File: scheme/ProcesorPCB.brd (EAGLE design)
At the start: 87.3 x 59.7 mm, 25 parts, among them X1 22-23-2101, X10 22-23-2021, X11 22-23-2021, X12 22-23-2051, X2 22-23-2101, X3 22-23-2101, X4 22-23-2101, X5 22-23-2051, X7 22-23-2021, X8 22-23-2031, X9 22-23-2021

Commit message: Work on PCB
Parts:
- removed X1, X2, X3, X4: 22-23-2101, con-molex:22-23-2101
- removed X10, X11, X7, X9: 22-23-2021, con-molex:22-23-2021
- removed X5: 22-23-2051, con-molex:22-23-2051
- removed X6: (no value), con-ptr500:AK500/2
- removed X8: 22-23-2031, con-molex:22-23-2031
- added JP10, JP11, JP12, JP13, JP14, JP15, JP16, JP17, JP18, JP7, JP8, JP9: (no value), jumper:JP2
- JP1: device jumper:JP4 -> jumper:JP10Q
- moved JP3 23.0 mm to (58.4, 41.9)
- moved JP1 21.0 mm to (78.7, 15.2), turned to 90 degrees
- moved X12 9.92 mm to (14.0, 8.89)
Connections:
- removed net DI: JP1.3, X5.1
- removed net DO: X5.4
- removed net E2: U$1.5, X1.9
- removed net E3: X2.4
- removed net E4: X2.9
- removed net E5: X3.4
- removed net E6: X3.9
- removed net E8: JP1.1, X4.9
- removed net EV11: X2.6
- removed net EV12: X2.8
- removed net EV17: X3.6
- removed net EV18: X3.8
- removed net N$29: X3.10
- removed net Y3: X2.5
- removed net Y4: X2.7
- removed net Y5: X3.5
- removed net Y6: X3.7
- new net CCP: JP1.6, U$1.5
- new net N$7: R1.1
- new net N$9: JP3.3, JP3.4, JP6.1
- net +5V: now also JP1.4; no longer R1.1, R2.1, X10.1, X11.1, X4.1, X6.1, X7.1, X9.1
- net CKL: no longer X5.2
- net E1: no longer X1.4
- net E7: no longer X4.6
- net EV5: no longer X1.6
- net EV6: no longer X1.8
- net GND: now also JP1.10; no longer JP3.3, JP3.4, JP6.1, X10.2, X11.2, X4.2, X5.5, X6.2, X7.2, X8.1, X9.2
- net LD: no longer X5.3
- net PGC,S1: no longer X1.2, X2.2, X3.2, X4.4
- net PGD,S2: no longer X1.1, X2.1, X3.1, X4.3
- net RX: no longer X8.2
- net S0: no longer X1.3, X2.3, X3.3, X4.5
- net SDA: no longer JP1.4
- net SDO: no longer JP1.2
- net TX: no longer X8.3
- net VPP,Y7: no longer X4.7
- net Y1: no longer X1.5
- net Y2: no longer X1.7
- net Y8: no longer X4.8
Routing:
- net GND: track 342.8 -> 0.00 mm, vias 2 -> 0
- net +5V: track 170.4 -> 0.00 mm
- net Y8: track 153.7 -> 0.00 mm
- net E7: track 151.1 -> 0.00 mm
- net VPP,Y7: track 149.9 -> 0.00 mm, vias 2 -> 0
- net E8: track 110.5 -> 0.00 mm, vias 2 -> 0
- net TX: track 95.2 -> 0.00 mm, vias 2 -> 0
- net E2: track 87.6 -> 0.00 mm
- net EV6: track 82.5 -> 0.00 mm
- net N$9: track 0.00 -> 78.7 mm
- net Y2: track 77.5 -> 0.00 mm
- net PGC,S1: track 71.1 -> 0.00 mm
- net PGD,S2: track 63.5 -> 0.00 mm
- net RX: track 76.2 -> 24.1 mm, vias 2 -> 0
- net S0: track 49.5 -> 0.00 mm
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
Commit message: Hmm not Saved
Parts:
- added U1: UA78L05ACPKG3, TI-Eagle_library:SOT150P400X160-4N
- added X1: 22-23-2031, con-molex:22-23-2031
- moved LED3 55.7 mm to (25.4, 26.7)
- moved R3 53.4 mm to (31.8, 28.6)
- moved JP3 23.0 mm to (35.6, 44.5), turned to 90 degrees
- moved JP1 1.27 mm to (77.5, 15.2)
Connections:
- removed net CKL: U$1.11
- removed net E1: U$1.16
- removed net E7: U$1.3
- removed net EV5: U$1.14
- removed net LD: U$1.8
- removed net N$7: R1.1
- removed net PGC,S1: U$1.18, X12.4
- removed net PGD,S2: U$1.19, X12.3
- removed net S0: U$1.17
- removed net SDA: U$1.13
- removed net SDO: U$1.9
- removed net Y1: U$1.15
- removed net Y2: U$1.7
- new net +24V: U1.3, X1.3
- new net AN0,PGD: JP7.2, U$1.19, X12.3
- new net AN1,PGC: JP8.2, U$1.18, X12.4
- new net AN10: JP17.2, U$1.13
- new net AN11: JP18.2, U$1.12
- new net AN2: JP9.2, U$1.17
- new net AN3: JP10.2, U$1.3
- new net AN4: JP11.2, U$1.16
- new net AN5: JP12.2, U$1.15
- new net AN6: JP13.2, U$1.14
- new net AN7: JP14.2, U$1.7
- new net AN8: JP15.2, U$1.8
- new net AN9: JP16.2, U$1.9
- new net OUT: U$1.11, X1.2
- net +5V: now also JP10.1, JP11.1, JP12.1, JP13.1, JP14.1, JP15.1, JP16.1, JP17.1, JP18.1, JP7.1, JP8.1, JP9.1, U1.1; no longer JP4.1, LED3.A
- net GND: now also JP10.3, JP11.3, JP12.3, JP13.3, JP14.3, JP15.3, JP16.3, JP17.3, JP18.3, JP7.3, JP8.3, JP9.3, U1.2, U1.4, X1.1; no longer R3.1
- net RX: no longer U$1.12
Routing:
- net GND: track 0.00 -> 63.5 mm
- net +5V: track 0.00 -> 51.3 mm
- net N$9: track 78.7 -> 58.6 mm
- net N$2: track 54.7 -> 35.6 mm
- net +24V: track 0.00 -> 16.8 mm
- net CCP: track 0.00 -> 12.7 mm
- net OUT: track 0.00 -> 10.2 mm
- net N$8: track 3.39 -> 0.00 mm

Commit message: PCB borad almost finished.
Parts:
- removed JP3, JP5, JP6: (no value), jumper:JP4
- removed JP4: (no value), jumper:JP1
- removed LED1: Cervena, led:LED5MM
- removed LED2, LED3: Zenena, led:LED5MM
- removed R2, R3: (no value), rcl:R0805W
- added C1: 1uF, resistor:C025-030X050
- added C2: 0.33uF, resistor:C025-030X050
- added RN1, RN2: 15K, resistor-net:RN-7
- added RN3: 22k, resistor-net:RN-7
- added RN4: 22K, resistor-net:RN-7
- R1: device rcl:R0805W -> resistor:0207/10
- moved R1 50.6 mm to (52.1, 21.6), flipped to the top, turned to 90 degrees
- moved X12 31.8 mm to (45.7, 10.2)
- moved JP2 22.5 mm to (50.8, 38.1), turned to 270 degrees
- moved X1 10.5 mm to (45.7, 29.2)
- moved JP1 5.08 mm to (82.5, 15.2)
- moved U1 1.80 mm to (57.1, 5.08)
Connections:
- removed net AN11: JP18.2, U$1.12
- removed net N$3: JP6.4, LED2.K
- removed net N$4: JP6.3, LED1.K
- removed net N$5: LED2.A, R2.2
- removed net N$6: LED1.A, R1.2
- removed net N$8: LED3.K, R3.2
- removed net N$9: JP3.3, JP3.4, JP6.1
- removed net RX: JP2.4, JP5.4
- new net AN11,RX: JP18.2, JP2.4, RN1.7, RN3.7, U$1.12
- net +24V: now also R1.2; no longer U1.3
- net +5V: now also C1.1, RN3.1, RN4.1
- net AN0,PGD: now also RN2.7, RN4.7
- net AN1,PGC: now also RN2.6, RN4.6
- net AN10: now also RN1.3, RN3.3
- net AN2: now also RN2.5, RN4.5
- net AN3: now also RN1.2, RN3.2
- net AN4: now also RN2.4, RN4.4
- net AN5: now also RN2.3, RN4.3
- net AN6: now also RN2.2, RN4.2
- net AN7: now also RN1.4, RN3.4
- net AN8: now also RN1.5, RN3.5
- net AN9: now also RN1.6, RN3.6
- net GND: now also C1.2, C2.2, JP2.2, RN1.1, RN2.1
- net N$2: now also C2.1, R1.1, U1.3; no longer JP3.1, JP3.2, JP4.2, JP6.2
- net TX: no longer JP5.3
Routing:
- net GND: track 63.5 -> 128.2 mm, vias 0 -> 1
- net N$9: track 58.6 -> 0.00 mm
- net AN10: track 0.00 -> 41.8 mm
- net AN3: track 0.00 -> 40.7 mm
- net AN0,PGD: track 0.00 -> 36.1 mm
- net AN1,PGC: track 0.00 -> 34.3 mm
- net AN2: track 0.00 -> 30.5 mm
- net AN4: track 0.00 -> 30.3 mm
- net AN5: track 0.00 -> 28.8 mm
- net +5V: track 51.3 -> 79.4 mm
- net AN11,RX: track 0.00 -> 25.5 mm
- net AN6: track 0.00 -> 25.5 mm
- net N$3: track 25.4 -> 0.00 mm
- net RX: track 24.1 -> 0.00 mm
- net AN7: track 0.00 -> 23.4 mm
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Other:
- board size 87.3 x 59.7 mm -> 44.1 x 45.7 mm

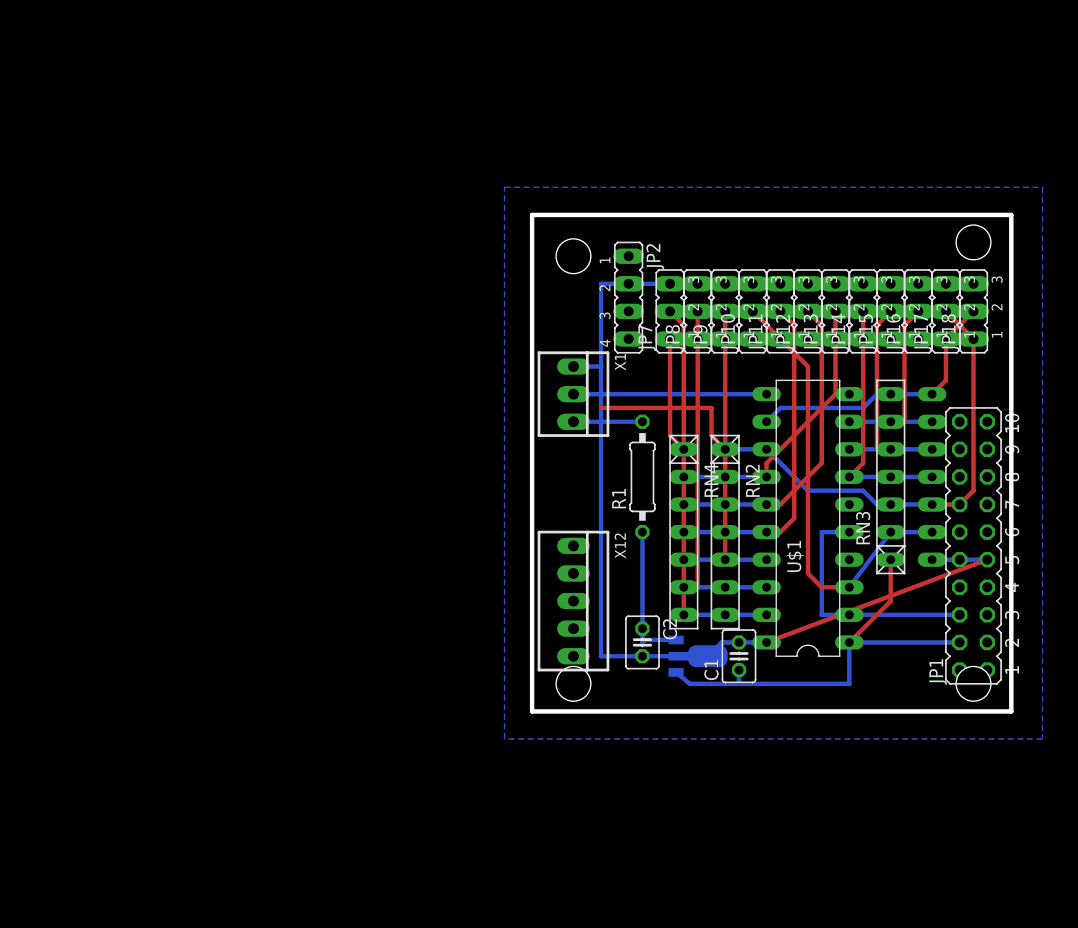
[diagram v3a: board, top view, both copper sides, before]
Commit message: Add documentation for LM358, update schema, add adc settings from previous project to file orig_mail.c
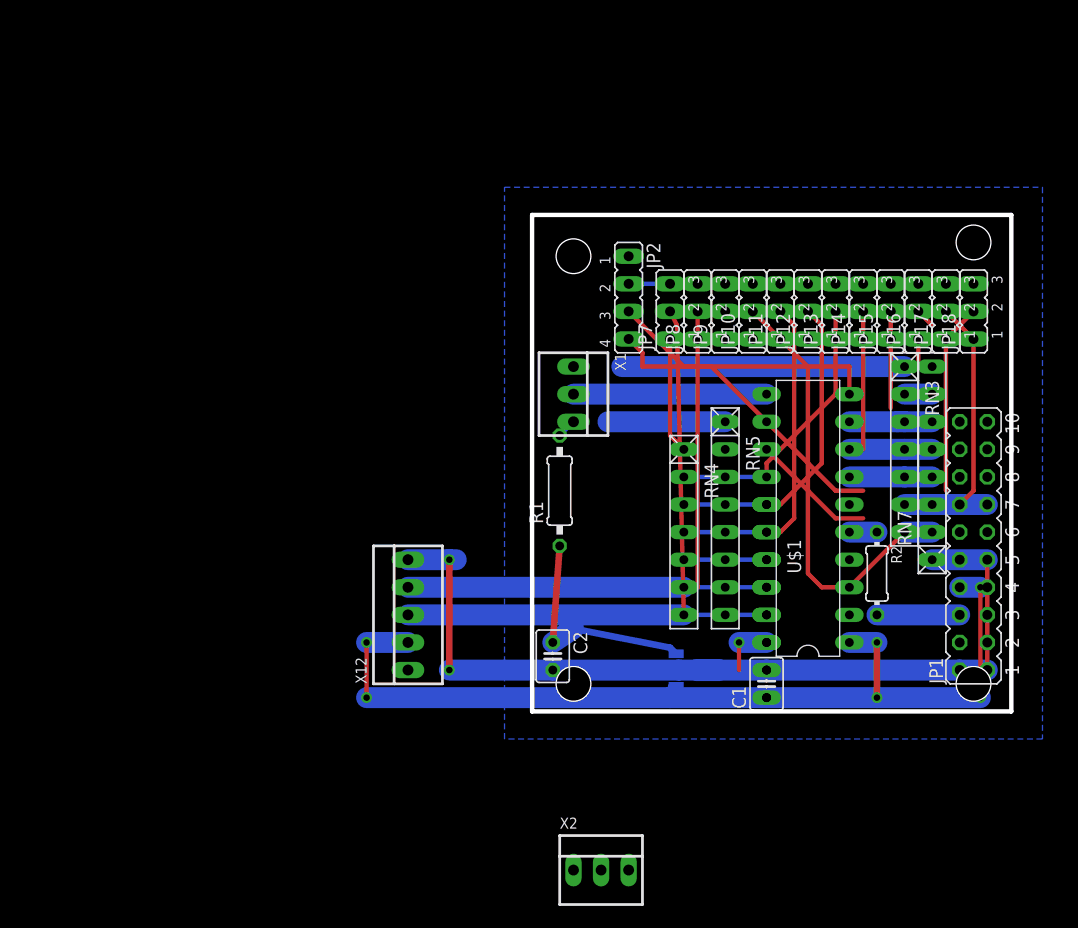
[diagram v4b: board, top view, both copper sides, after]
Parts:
- removed RN2: 15K, resistor-net:RN-7
- added R2: 1k, resistor:0204/7
- added RN5: 15k, resistor-net:RN-8
- added RN7: (no value), resistor-net:RN-8
- added X2: 22-23-2031, con-molex:22-23-2031
- RN1: value 15K -> 15k; device resistor-net:RN-7 -> resistor-net:RN-8
- moved RN1 19.0 mm to (63.5, 10.2), turned to 270 degrees
- moved X12 15.3 mm to (30.5, 8.89), turned to 90 degrees
- moved C2 8.35 mm to (43.8, 5.08)
- moved R1 7.73 mm to (44.5, 20.3)
- moved C1 3.59 mm to (63.5, 2.54)
- moved RN3 2.84 mm to (76.2, 24.1), turned to 270 degrees
- moved U1 1.27 mm to (57.1, 3.81)
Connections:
- new net N$4: JP1.6, R2.2
- net +5V: now also JP1.8, RN1.8; no longer JP1.4
- net AN0,PGD: no longer RN2.7
- net AN1,PGC: no longer RN2.6
- net AN10: now also RN3.6, RN7.3; no longer RN1.3, RN3.3
- net AN11,RX: now also RN3.2, RN7.7, X2.2; no longer RN1.7, RN3.7
- net AN2: no longer RN2.5
- net AN3: now also RN3.7, RN7.2; no longer RN1.2, RN3.2
- net AN4: no longer RN2.4
- net AN5: no longer RN2.3
- net AN6: no longer RN2.2
- net AN7: now also RN3.5, RN7.4; no longer RN1.4, RN3.4
- net AN8: now also RN3.4, RN7.5; no longer RN1.5, RN3.5
- net AN9: now also RN3.3, RN7.6; no longer RN1.6, RN3.6
- net CCP: now also R2.1; no longer JP1.6
- net GND: now also JP1.2, RN1.7, RN5.1, RN7.1, X2.1; no longer JP1.10, RN1.1, RN2.1
- net TX: now also X2.3
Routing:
- net +5V: track 79.4 -> 153.9 mm, vias 0 -> 6
- net AN1,PGC: track 34.3 -> 59.7 mm
- net AN0,PGD: track 36.1 -> 61.1 mm
- net TX: track 0.00 -> 25.0 mm
- net AN2: track 30.5 -> 7.62 mm
- net AN11,RX: track 25.5 -> 48.2 mm
- net CCP: track 22.9 -> 2.54 mm
- net AN9: track 19.6 -> 9.42 mm
- net N$2: track 13.4 -> 21.1 mm
- net N$4: track 0.00 -> 7.62 mm
- net AN8: track 22.1 -> 16.5 mm
- net +24V: track 6.35 -> 1.80 mm
- net AN10: track 41.8 -> 38.5 mm
- net AN7: track 23.4 -> 20.3 mm
- net GND: track 128.2 -> 127.0 mm, vias 1 -> 5
